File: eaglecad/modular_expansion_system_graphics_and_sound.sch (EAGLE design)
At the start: 55 parts, among them IC1 74LS244N, IC2 ATF22V10, IC3 74LS74N, IC8 74LS244N, IC9-74HCU04 74LS04N, J1-INTERRUPTS INTERRUPTS, J1_ADDRESS_CON j1, J2-WAITS WAITS, J2_DATA_AND_POWER_CON j2, J3-VIDEO-OUT RCA, J4-AUDIO-LEFT RCA, J5-AUDIO-RIGHT RCA, Q2 2N2222, U1 TMS4416, U11 SN76489, U2 TMS9118, U3 TMS4416, U4 SN76489, U5 SN76489, U6 SN76489, Y1 OSC1-CPP-4

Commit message: updated readme and minor updates to schematic for gs board
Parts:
- renumbered IC1 to IC1_JOY2_BUF, IC2 to IC2_GLU, IC8 to IC8_JOY1_BUF, U1 to U1_TMS_RAM, U11 to U11_SND1, U2 to U2_VDP, U3 to U3_TMS_RAM, U4 to U4_SND2, U5 to U5_SND3, U6 to U6_SND4
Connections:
- net N$11 renamed SND4_ENABLE_N
- net N$15 renamed SND4_READY
- net N$8 renamed SND3_READY
- net N$9 renamed SND3_ENABLE_N

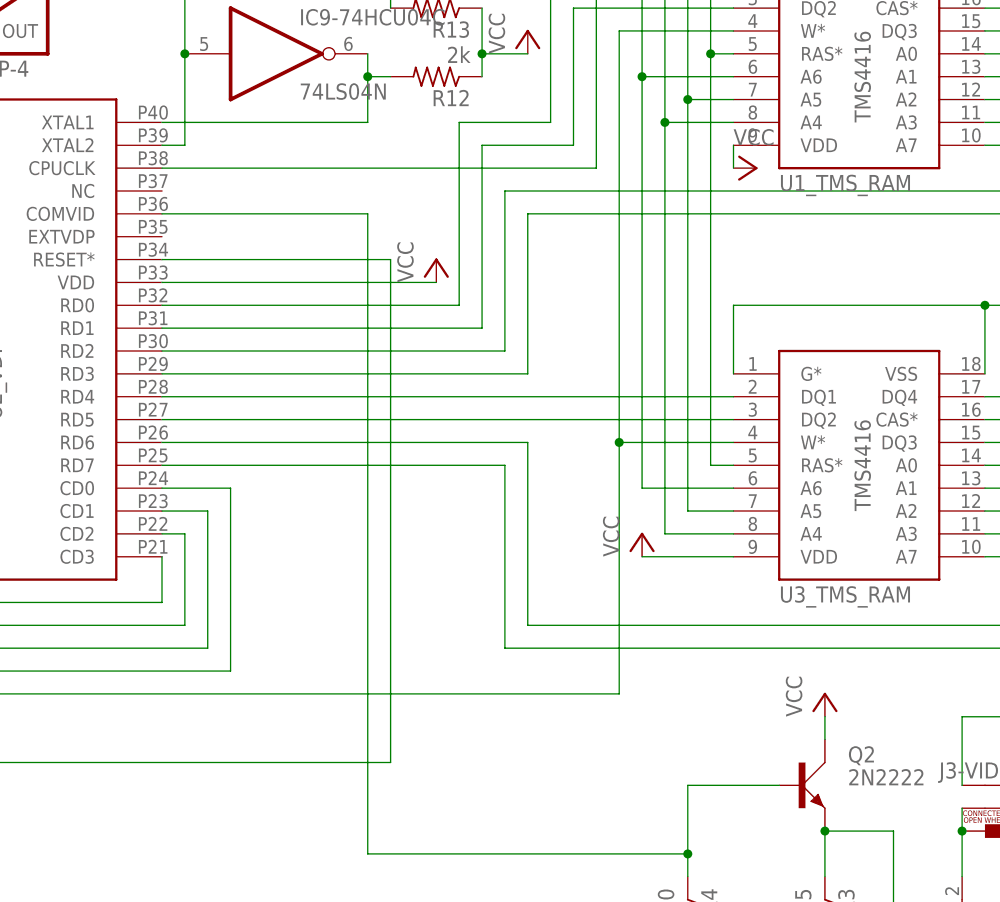
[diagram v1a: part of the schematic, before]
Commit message: added inductor to grfx brd and removed extra 7805
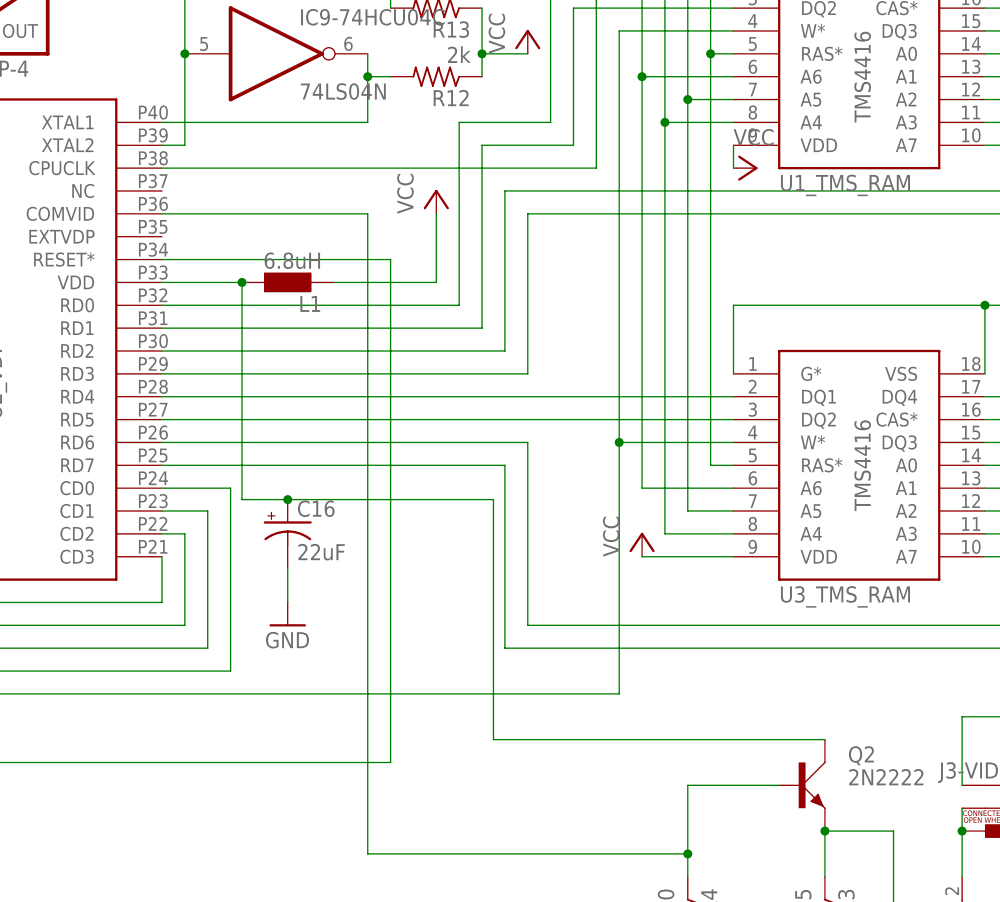
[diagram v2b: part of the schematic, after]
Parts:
- added C16: 22uF, resistor:CPOL-USE2.5-5
- added L1: 6.8uH, eagle-ltspice:L0207/10
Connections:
- new net VID-VCC: C16.+, L1.1, Q2.C, U2_VDP.VDD
- net GND: now also C16.-
- net VCC: now also L1.2; no longer Q2.C, U2_VDP.VDD
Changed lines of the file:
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@@
 <setting verticaltext="up"/>
 </settings>
-<grid distance="0.1" unitdist="inch" unit="inch" style="lines" multiple="1" display="no" altdistance="0.01" altunitdist="inch" altunit="inch"/>
+<grid distance="0.05" unitdist="inch" unit="inch" style="lines" multiple="1" display="no" altdistance="0.005" altunitdist="inch" altunit="inch"/>
 <layers>
 <layer number="1" name="Top" color="4" fill="1" visible="no" active="no"/>
@@
 <part name="J5-AUDIO-RIGHT" library="SparkFun-Connectors" deviceset="RCA" device=""/>
 <part name="Q2" library="transistor-small-signal" library_urn="urn:adsk.eagle:library:401" deviceset="2N2222" device="" package3d_urn="urn:adsk.eagle:package:29734/2"/>
-<part name="P+5" library="supply1" library_urn="urn:adsk.eagle:library:371" deviceset="VCC" device=""/>
 <part name="GND10" library="supply1" library_urn="urn:adsk.eagle:library:371" deviceset="GND" device=""/>
 <part name="R3" library="resistor" library_urn="urn:adsk.eagle:library:348" deviceset="R-US_" device="0207/2V" package3d_urn="urn:adsk.eagle:package:23490/1" value="75"/>
@@
 <part name="R2" library="resistor" library_urn="urn:adsk.eagle:library:348" deviceset="R-US_" device="0207/2V" package3d_urn="urn:adsk.eagle:package:23490/1" value="150k"/>
 <part name="R6" library="resistor" library_urn="urn:adsk.eagle:library:348" deviceset="R-US_" device="0207/2V" package3d_urn="urn:adsk.eagle:package:23490/1" value="150k"/>
+<part name="L1" library="eagle-ltspice" library_urn="urn:adsk.eagle:library:217" deviceset="L" device="0207/10" package3d_urn="urn:adsk.eagle:package:13275/1" value="6.8uH"/>
+<part name="C16" library="resistor" library_urn="urn:adsk.eagle:library:348" deviceset="CPOL-US" device="E2.5-5" package3d_urn="urn:adsk.eagle:package:23344/1" value="22uF"/>
+<part name="GND14" library="supply1" library_urn="urn:adsk.eagle:library:371" deviceset="GND" device=""/>
 </parts>
 <sheets>
@@
 <attribute name="VALUE" x="229.87" y="77.47" size="1.778" layer="96"/>
 </instance>
-<instance part="P+11" gate="VCC" x="323.85" y="95.25" smashed="yes">
-<attribute name="VALUE" x="321.31" y="92.71" size="1.778" layer="96" rot="R90"/>
+<instance part="P+11" gate="VCC" x="323.85" y="102.87" smashed="yes">
+<attribute name="VALUE" x="321.31" y="100.33" size="1.778" layer="96" rot="R90"/>
 </instance>
 <instance part="H1" gate="G$1" x="54.61" y="156.21" smashed="yes" rot="R90">
@@
 <attribute name="VALUE" x="369.57" y="36.83" size="1.778" layer="96"/>
 </instance>
-<instance part="P+5" gate="VCC" x="367.03" y="46.99" smashed="yes">
-<attribute name="VALUE" x="364.49" y="44.45" size="1.778" layer="96" rot="R90"/>
-</instance>
 <instance part="GND10" gate="1" x="382.27" y="11.43" smashed="yes">
 <attribute name="VALUE" x="379.73" y="8.89" size="1.778" layer="96"/>
@@
 <attribute name="NAME" x="387.35" y="253.7714" size="1.778" layer="95" rot="R180"/>
 <attribute name="VALUE" x="387.35" y="258.572" size="1.778" layer="96" rot="R180"/>
+</instance>
+<instance part="L1" gate="G$1" x="307.34" y="92.71" smashed="yes" rot="R90">
+<attribute name="NAME" x="311.15" y="91.2114" size="1.778" layer="95" rot="R180"/>
+<attribute name="VALUE" x="311.15" y="96.012" size="1.778" layer="96" rot="R180"/>
+</instance>
+<instance part="C16" gate="G$1" x="307.34" y="66.04" smashed="yes">
+<attribute name="NAME" x="308.356" y="66.675" size="1.778" layer="95"/>
+<attribute name="VALUE" x="308.356" y="61.849" size="1.778" layer="96"/>
+</instance>
+<instance part="GND14" gate="1" x="307.34" y="54.61" smashed="yes">
+<attribute name="VALUE" x="304.8" y="52.07" size="1.778" layer="96"/>
 </instance>
 </instances>
@@
 <wire x1="408.94" y1="261.62" x2="408.94" y2="259.08" width="0.1524" layer="91"/>
 </segment>
+<segment>
+<pinref part="C16" gate="G$1" pin="-"/>
+<pinref part="GND14" gate="1" pin="GND"/>
+<wire x1="307.34" y1="60.96" x2="307.34" y2="57.15" width="0.1524" layer="91"/>
+</segment>
 </net>
 <net name="VCC" class="0">
-<segment>
-<pinref part="P+11" gate="VCC" pin="VCC"/>
-<wire x1="323.85" y1="92.71" x2="293.37" y2="92.71" width="0.1524" layer="91"/>
-<pinref part="U2_VDP" gate="G$1" pin="VDD"/>
-</segment>
 <segment>
 <pinref part="P+13" gate="VCC" pin="VCC"/>
@@
 <pinref part="U4_SND2" gate="G$1" pin="VCC"/>
 <wire x1="435.61" y1="217.17" x2="435.61" y2="212.09" width="0.1524" layer="91"/>
-</segment>
-<segment>
-<pinref part="P+5" gate="VCC" pin="VCC"/>
-<pinref part="Q2" gate="1" pin="C"/>
-<wire x1="367.03" y1="44.45" x2="367.03" y2="41.91" width="0.1524" layer="91"/>
 </segment>
 <segment>
@@
 <junction x="347.98" y="273.05"/>
 </segment>
+<segment>
+<pinref part="L1" gate="G$1" pin="2"/>
+<wire x1="312.42" y1="92.71" x2="323.85" y2="92.71" width="0.1524" layer="91"/>
+<pinref part="P+11" gate="VCC" pin="VCC"/>
+<wire x1="323.85" y1="92.71" x2="323.85" y2="100.33" width="0.1524" layer="91"/>
+</segment>
 </net>
 <net name="COMVID-OUT" class="0">
@@
 </segment>
 </net>
+<net name="VID-VCC" class="0">
+<segment>
+<pinref part="U2_VDP" gate="G$1" pin="VDD"/>
+<pinref part="L1" gate="G$1" pin="1"/>
+<wire x1="293.37" y1="92.71" x2="302.26" y2="92.71" width="0.1524" layer="91"/>
+<pinref part="C16" gate="G$1" pin="+"/>
+<wire x1="302.26" y1="92.71" x2="302.26" y2="68.58" width="0.1524" layer="91"/>
+<wire x1="302.26" y1="68.58" x2="307.34" y2="68.58" width="0.1524" layer="91"/>
+<junction x="302.26" y="92.71"/>
+<wire x1="307.34" y1="68.58" x2="330.2" y2="68.58" width="0.1524" layer="91"/>
+<junction x="307.34" y="68.58"/>
+<wire x1="330.2" y1="68.58" x2="330.2" y2="41.91" width="0.1524" layer="91"/>
+<pinref part="Q2" gate="1" pin="C"/>
+<wire x1="330.2" y1="41.91" x2="367.03" y2="41.91" width="0.1524" layer="91"/>
+</segment>
+</net>

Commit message: tweaked graphics card to match older TRS80 joysticks and tweaked pacman game
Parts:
- added D1, D2, D3, D7: (1N821), rcl:R-US_0204/2V
- added JP2-TRIGGER-MODE, JP2-TRIGGER-MODE1: (no value), jumper:JP2E
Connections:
- removed net N$99: IC1_JOY2_BUFB.A2, IC1_JOY2_BUFB.A3, IC1_JOY2_BUFB.A4, IC8_JOY1_BUFB.A2, IC8_JOY1_BUFB.A3, IC8_JOY1_BUFB.A4, RN1.8
- new net 5_BIT_TRIGGER_LINE: IC8_JOY1_BUFA.A4, JP2-TRIGGER-MODE.1, RN1.12
- new net 5_BIT_TRIGGER_LINE_2: IC1_JOY2_BUFA.A4, JP2-TRIGGER-MODE1.1, RN1.6
- new net N$11: IC8_JOY1_BUFA.A1, IC8_JOY1_BUFA.A2, IC8_JOY1_BUFA.A3, RN1.13
- new net N$20: IC1_JOY2_BUFA.A1, IC1_JOY2_BUFA.A2, IC1_JOY2_BUFA.A3, RN1.7
- new net TOPOFDIODES: D1.1, D2.1, JP2-TRIGGER-MODE.3
- new net TOPOFDIODES1: D3.1, D7.1, JP2-TRIGGER-MODE1.3
- net DOWN: now also D2.2, IC8_JOY1_BUFB.A3, RN1.11; no longer IC8_JOY1_BUFA.A2, RN1.12
- net DOWN1: now also D7.2, IC1_JOY2_BUFB.A3, RN1.5; no longer IC1_JOY2_BUFA.A2, RN1.6
- net LEFT: now also IC8_JOY1_BUFB.A2, RN1.8; no longer IC8_JOY1_BUFA.A3, RN1.11
- net LEFT1: now also IC1_JOY2_BUFB.A2, RN1.2; no longer IC1_JOY2_BUFA.A3, RN1.5
- net RIGHT: now also IC8_JOY1_BUFB.A1, RN1.9; no longer IC8_JOY1_BUFA.A4, RN1.10
- net RIGHT1: now also IC1_JOY2_BUFB.A1, RN1.3; no longer IC1_JOY2_BUFA.A4, RN1.4
- net TRIGGER: now also JP2-TRIGGER-MODE.2; no longer IC8_JOY1_BUFB.A1, RN1.9
- net TRIGGER1: now also JP2-TRIGGER-MODE1.2; no longer IC1_JOY2_BUFB.A1, RN1.3
- net UP: now also D1.2, IC8_JOY1_BUFB.A4, RN1.10; no longer IC8_JOY1_BUFA.A1, RN1.13
- net UP1: now also D3.2, IC1_JOY2_BUFB.A4, RN1.4; no longer IC1_JOY2_BUFA.A1, RN1.7
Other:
- moved on the sheet: H1, H3, H4, H5, JOYSTICK1, JOYSTICK2, RN1

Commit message: joystick pin fixes to match old alphastick
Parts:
- JP1-TRG-MD2: value (none) -> JP1
- JP2-TRG-MD1: value (none) -> JP2
- renumbered JP1 to JP1-INTRPT, JP2-TRIGGER-MODE to JP2-TRG-MD1, JP2-TRIGGER-MODE1 to JP1-TRG-MD2
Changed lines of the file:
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@@
 <part name="RN1" library="resistor-sil" library_urn="urn:adsk.eagle:library:347" deviceset="G12R" device="" package3d_urn="urn:adsk.eagle:package:25289/1" value="4.7k"/>
 <part name="P+6" library="supply1" library_urn="urn:adsk.eagle:library:371" deviceset="VCC" device=""/>
-<part name="JP1" library="jumper" library_urn="urn:adsk.eagle:library:252" deviceset="JP1E" device="" package3d_urn="urn:adsk.eagle:package:15455/1" value="INT__VDP_JP"/>
+<part name="JP1-INTRPT" library="jumper" library_urn="urn:adsk.eagle:library:252" deviceset="JP1E" device="" package3d_urn="urn:adsk.eagle:package:15455/1" value="INT__VDP_JP"/>
 <part name="R8" library="resistor" library_urn="urn:adsk.eagle:library:348" deviceset="R-TRIMM" device="64W" package3d_urn="urn:adsk.eagle:package:23748/1" value="400"/>
 <part name="R9" library="resistor" library_urn="urn:adsk.eagle:library:348" deviceset="R-US_" device="0207/2V" package3d_urn="urn:adsk.eagle:package:23490/1" value="4.7k"/>
@@
 <part name="C16" library="resistor" library_urn="urn:adsk.eagle:library:348" deviceset="CPOL-US" device="E2.5-5" package3d_urn="urn:adsk.eagle:package:23344/1" value="22uF"/>
 <part name="GND14" library="supply1" library_urn="urn:adsk.eagle:library:371" deviceset="GND" device=""/>
-<part name="JP2-TRIGGER-MODE" library="jumper" library_urn="urn:adsk.eagle:library:252" deviceset="JP2E" device="" package3d_urn="urn:adsk.eagle:package:15452/1"/>
-<part name="JP2-TRIGGER-MODE1" library="jumper" library_urn="urn:adsk.eagle:library:252" deviceset="JP2E" device="" package3d_urn="urn:adsk.eagle:package:15452/1"/>
+<part name="JP2-TRG-MD1" library="jumper" library_urn="urn:adsk.eagle:library:252" deviceset="JP2E" device="" package3d_urn="urn:adsk.eagle:package:15452/1" value="JP2"/>
+<part name="JP1-TRG-MD2" library="jumper" library_urn="urn:adsk.eagle:library:252" deviceset="JP2E" device="" package3d_urn="urn:adsk.eagle:package:15452/1" value="JP1"/>
 <part name="D7" library="rcl" library_urn="urn:adsk.eagle:library:334" deviceset="R-US_" device="0204/2V" package3d_urn="urn:adsk.eagle:package:23495/1" value="(1N821)"/>
 <part name="D3" library="rcl" library_urn="urn:adsk.eagle:library:334" deviceset="R-US_" device="0204/2V" package3d_urn="urn:adsk.eagle:package:23495/1" value="(1N821)"/>
@@
 <attribute name="VALUE" x="158.75" y="156.21" size="1.778" layer="96" rot="R90"/>
 </instance>
-<instance part="JP1" gate="A" x="199.39" y="283.21" smashed="yes" rot="R270">
+<instance part="JP1-INTRPT" gate="A" x="199.39" y="283.21" smashed="yes" rot="R270">
 <attribute name="NAME" x="196.85" y="274.32" size="1.778" layer="95"/>
 <attribute name="VALUE" x="199.39" y="277.495" size="1.778" layer="96"/>
@@
 <attribute name="VALUE" x="304.8" y="52.07" size="1.778" layer="96"/>
 </instance>
-<instance part="JP2-TRIGGER-MODE" gate="1" x="116.84" y="232.41" smashed="yes" rot="R270">
+<instance part="JP2-TRG-MD1" gate="1" x="116.84" y="232.41" smashed="yes" rot="R270">
 <attribute name="NAME" x="116.84" y="236.22" size="1.778" layer="95"/>
 <attribute name="VALUE" x="116.84" y="226.695" size="1.778" layer="96"/>
 </instance>
-<instance part="JP2-TRIGGER-MODE1" gate="1" x="116.84" y="182.88" smashed="yes" rot="R270">
+<instance part="JP1-TRG-MD2" gate="1" x="116.84" y="182.88" smashed="yes" rot="R270">
 <attribute name="NAME" x="116.84" y="186.69" size="1.778" layer="95"/>
 <attribute name="VALUE" x="116.84" y="177.165" size="1.778" layer="96"/>
@@
 <label x="101.6" y="232.41" size="1.778" layer="95"/>
 <wire x1="114.3" y1="232.41" x2="97.79" y2="232.41" width="0.1524" layer="91"/>
-<pinref part="JP2-TRIGGER-MODE" gate="1" pin="2"/>
+<pinref part="JP2-TRG-MD1" gate="1" pin="2"/>
 </segment>
 </net>
@@
 <pinref part="JOYSTICK2" gate="G$1" pin="9"/>
 <wire x1="97.79" y1="182.88" x2="114.3" y2="182.88" width="0.1524" layer="91"/>
-<pinref part="JP2-TRIGGER-MODE1" gate="1" pin="2"/>
+<pinref part="JP1-TRG-MD2" gate="1" pin="2"/>
 </segment>
 </net>
@@
 <wire x1="257.81" y1="72.39" x2="245.11" y2="72.39" width="0.1524" layer="91"/>
 <wire x1="245.11" y1="72.39" x2="245.11" y2="41.91" width="0.1524" layer="91"/>
-<pinref part="JP1" gate="A" pin="2"/>
+<pinref part="JP1-INTRPT" gate="A" pin="2"/>
 <wire x1="245.11" y1="41.91" x2="196.85" y2="41.91" width="0.1524" layer="91"/>
 <wire x1="196.85" y1="41.91" x2="196.85" y2="280.67" width="0.1524" layer="91"/>
@@
 <segment>
 <pinref part="J1-INTERRUPTS" gate="G$1" pin="3"/>
-<pinref part="JP1" gate="A" pin="1"/>
+<pinref part="JP1-INTRPT" gate="A" pin="1"/>
 <wire x1="203.2" y1="302.26" x2="196.85" y2="302.26" width="0.1524" layer="91"/>
 <wire x1="196.85" y1="302.26" x2="196.85" y2="283.21" width="0.1524" layer="91"/>
@@
 <pinref part="IC8_JOY1_BUF" gate="A" pin="A4"/>
 <wire x1="161.29" y1="242.57" x2="148.59" y2="242.57" width="0.1524" layer="91"/>
-<pinref part="JP2-TRIGGER-MODE" gate="1" pin="1"/>
+<pinref part="JP2-TRG-MD1" gate="1" pin="1"/>
 <wire x1="148.59" y1="242.57" x2="114.3" y2="242.57" width="0.1524" layer="91"/>
 <wire x1="114.3" y1="242.57" x2="114.3" y2="234.95" width="0.1524" layer="91"/>
@@
 <segment>
 <pinref part="IC1_JOY2_BUF" gate="A" pin="A4"/>
-<pinref part="JP2-TRIGGER-MODE1" gate="1" pin="1"/>
+<pinref part="JP1-TRG-MD2" gate="1" pin="1"/>
 <wire x1="161.29" y1="194.31" x2="133.35" y2="194.31" width="0.1524" layer="91"/>
 <wire x1="133.35" y1="194.31" x2="114.3" y2="194.31" width="0.1524" layer="91"/>
@@
 <pinref part="D7" gate="G$1" pin="1"/>
 <wire x1="110.49" y1="177.8" x2="114.3" y2="177.8" width="0.1524" layer="91"/>
-<pinref part="JP2-TRIGGER-MODE1" gate="1" pin="3"/>
+<pinref part="JP1-TRG-MD2" gate="1" pin="3"/>
 <wire x1="114.3" y1="177.8" x2="114.3" y2="180.34" width="0.1524" layer="91"/>
 <pinref part="D3" gate="G$1" pin="1"/>
@@
 <pinref part="D1" gate="G$1" pin="1"/>
 <wire x1="114.3" y1="227.33" x2="114.3" y2="223.52" width="0.1524" layer="91"/>
-<pinref part="JP2-TRIGGER-MODE" gate="1" pin="3"/>
+<pinref part="JP2-TRG-MD1" gate="1" pin="3"/>
 <wire x1="114.3" y1="229.87" x2="114.3" y2="227.33" width="0.1524" layer="91"/>
 <junction x="114.3" y="227.33"/>
